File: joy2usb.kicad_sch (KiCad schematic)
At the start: 16 parts, among them J1 DB9_Male, J2 Conn_02x04_Odd_Even, SW1 RST, SW2 SW_SPDT, U1 Arduino_Pro_Micro, U2 4066

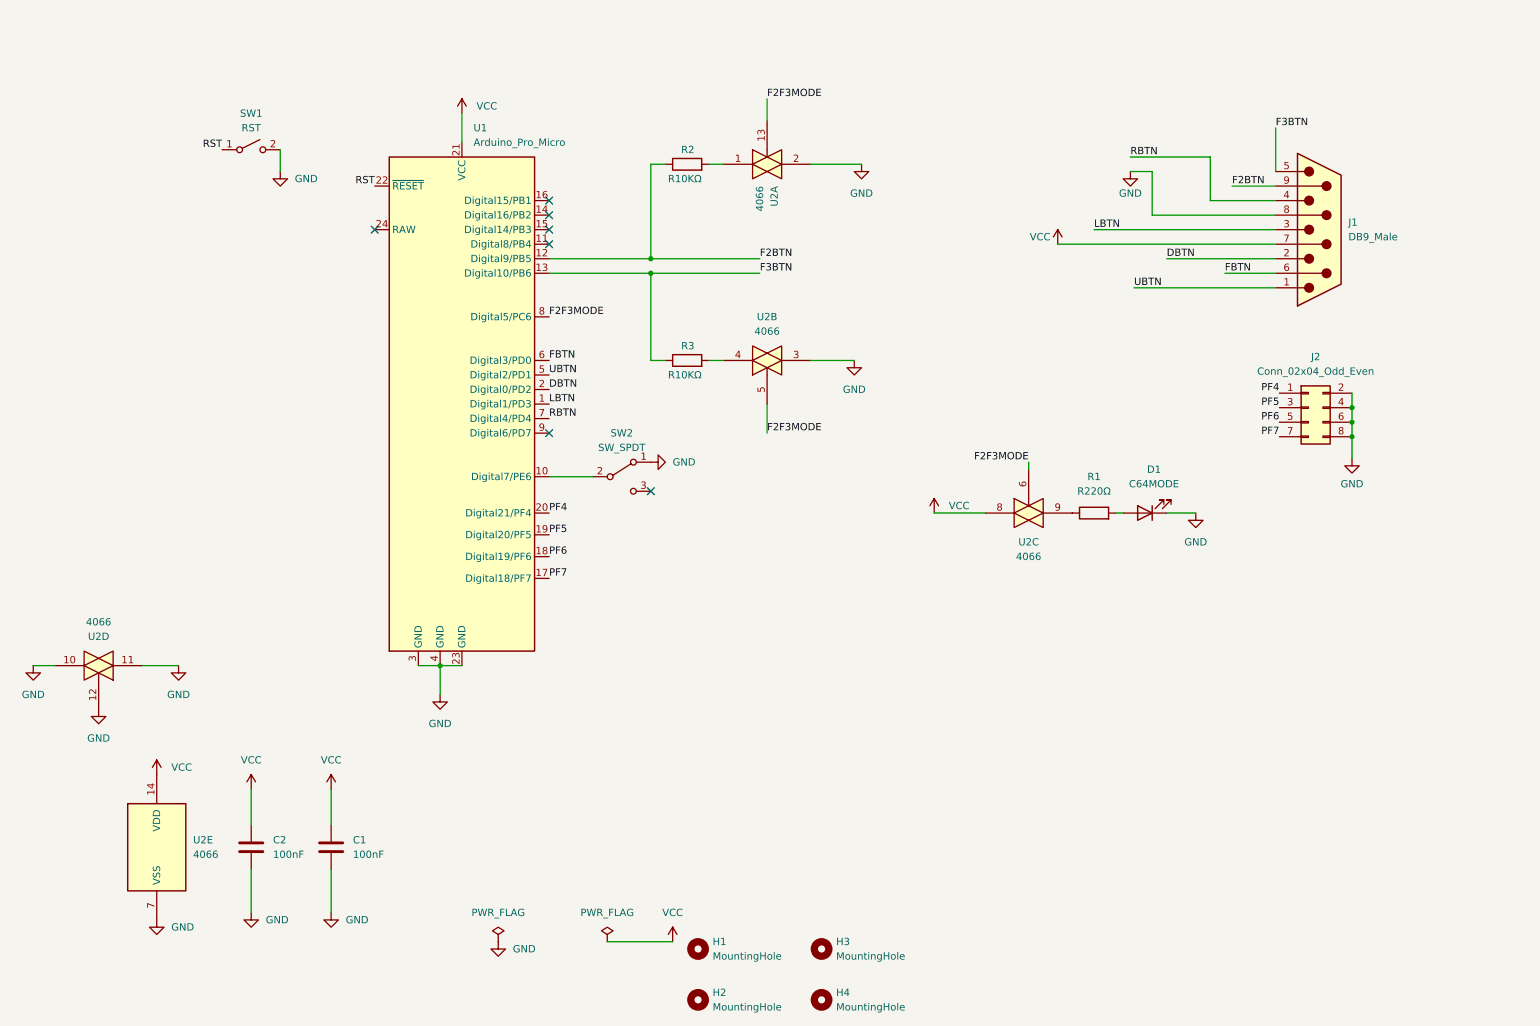
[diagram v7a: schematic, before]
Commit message: PCB Rev. 6.2
removal of ic 4066
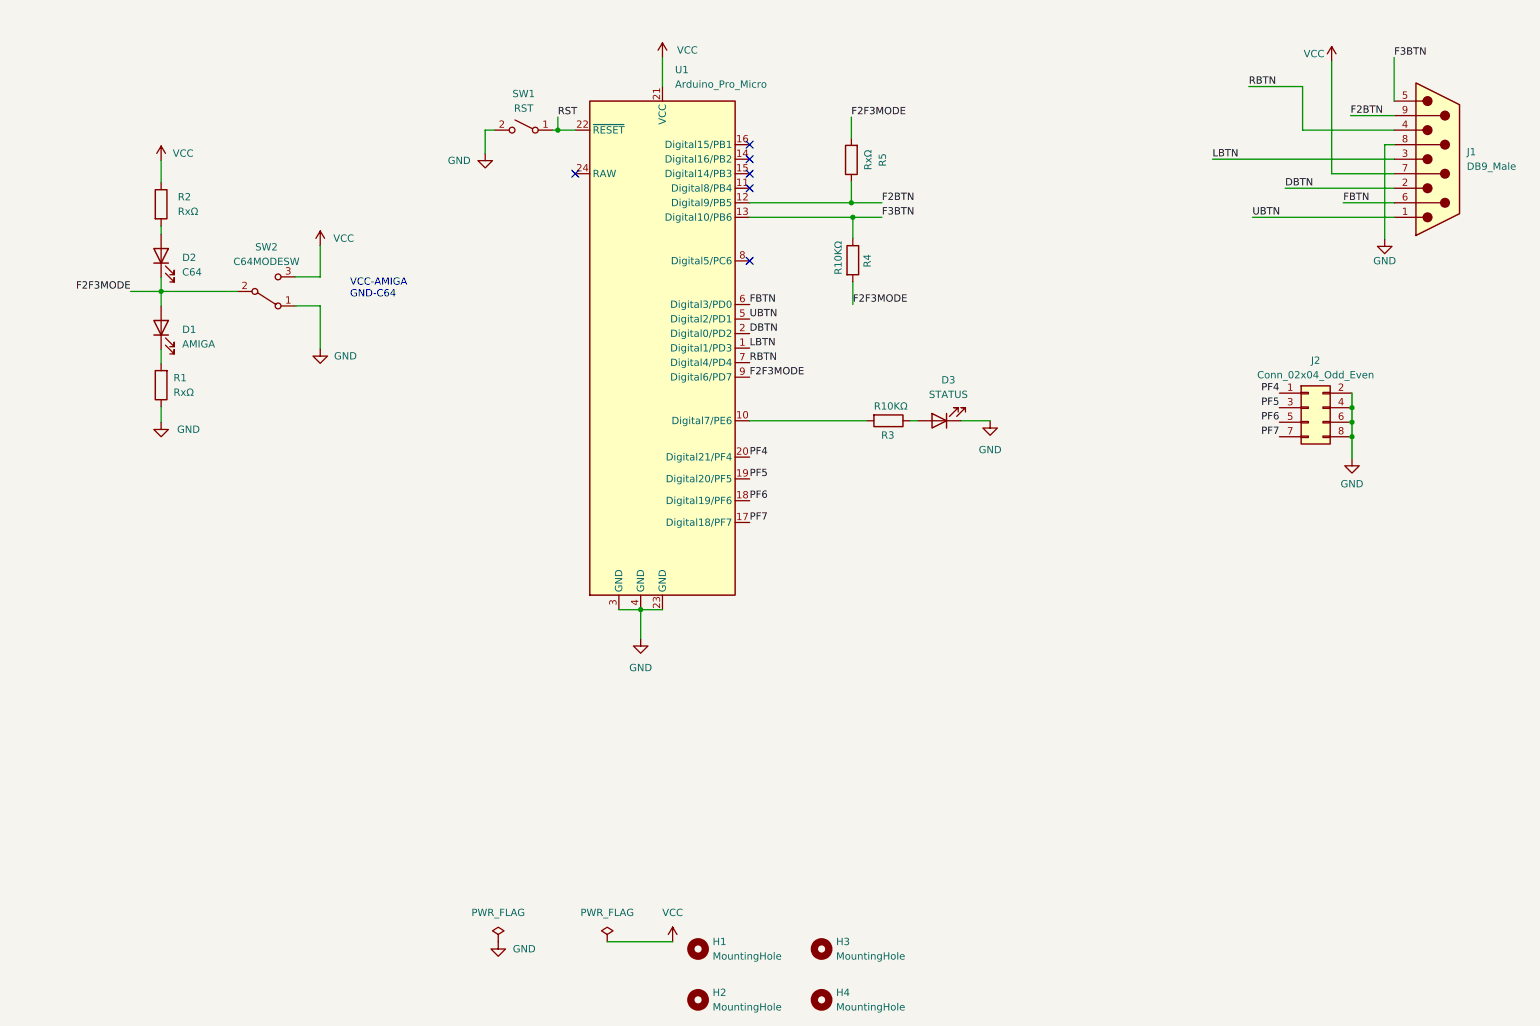
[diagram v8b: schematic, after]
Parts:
- removed C1, C2: 100nF, Capacitor_THT:C_Disc_D3.8mm_W2.6mm_P2.50mm, symbol Device:C
- removed U2: 4066, Package_DIP:DIP-14_W7.62mm_Socket_LongPads, symbol 4xxx:4066
- added D2: C64, misc:LED_D3.0mm_Oval, symbol Device:LED
- added D3: STATUS, misc:LED_D3.0mm_Oval, symbol Device:LED
- added R4: R10KΩ, misc:R_Axial_DIN0207_L6.3mm_D2.5mm_P10.16mm_Horizontal_Oval, symbol Device:R
- added R5: RxΩ, misc:R_Axial_DIN0207_L6.3mm_D2.5mm_P10.16mm_Horizontal_Oval, symbol Device:R
- D1: value C64MODE -> AMIGA; footprint Misc:LED_D3.0mm_Oval -> misc:LED_D3.0mm_Oval
- J1: symbol Connector:DB9_Male -> Connector:DE9_Plug
- R1: value R220Ω -> RxΩ; footprint Resistor_THT:R_Axial_DIN0207_L6.3mm_D2.5mm_P10.16mm_Horizontal -> misc:R_Axial_DIN0207_L6.3mm_D2.5mm_P10.16mm_Horizontal_Oval
- R2: value R10KΩ -> RxΩ; footprint Resistor_THT:R_Axial_DIN0207_L6.3mm_D2.5mm_P10.16mm_Horizontal -> misc:R_Axial_DIN0207_L6.3mm_D2.5mm_P10.16mm_Horizontal_Oval
- R3: footprint Resistor_THT:R_Axial_DIN0207_L6.3mm_D2.5mm_P10.16mm_Horizontal -> misc:R_Axial_DIN0207_L6.3mm_D2.5mm_P10.16mm_Horizontal_Oval
- SW2: value SW_SPDT -> C64MODESW; footprint Misc:MFP_1220_KNITTER_SWITCH_SPDT_Oval -> misc:E-Switch-EG1218-Manufacturer_Recommended_Oval
- U1: symbol Misc:Arduino_Pro_Micro -> misc:Arduino_Pro_Micro
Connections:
- net F2BTN: now also R5.1; no longer R2.1
- net F2F3MODE: now also D1.2 (A), SW2.2 (B), U1.9 (Digital6/PD7), D2.1 (K), R4.2, R5.2; no longer U1.8 (Digital5/PC6)
- net F3BTN: now also R4.1; no longer R3.1
- net GND: now also R1.1, D3.1 (K); no longer D1.1 (K)
- net VCC: now also R2.1, SW2.3 (C)
- net at R1.2: now also D1.1 (K); no longer D1.2 (A)
- net at U1.10 (Digital7/PE6): now also R3.2; no longer SW2.2 (B)
- net at R2.2: now also D2.2 (A)
- new net: D3.2 (A), R3.1
- no-connect marks 7 -> 6
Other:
- note added: "VCC-AMIGA GND-C64"
- moved on the sheet: J1, SW1, U1
